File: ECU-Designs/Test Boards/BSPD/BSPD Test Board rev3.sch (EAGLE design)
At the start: 30 parts, among them X1 CONNECTOR-10

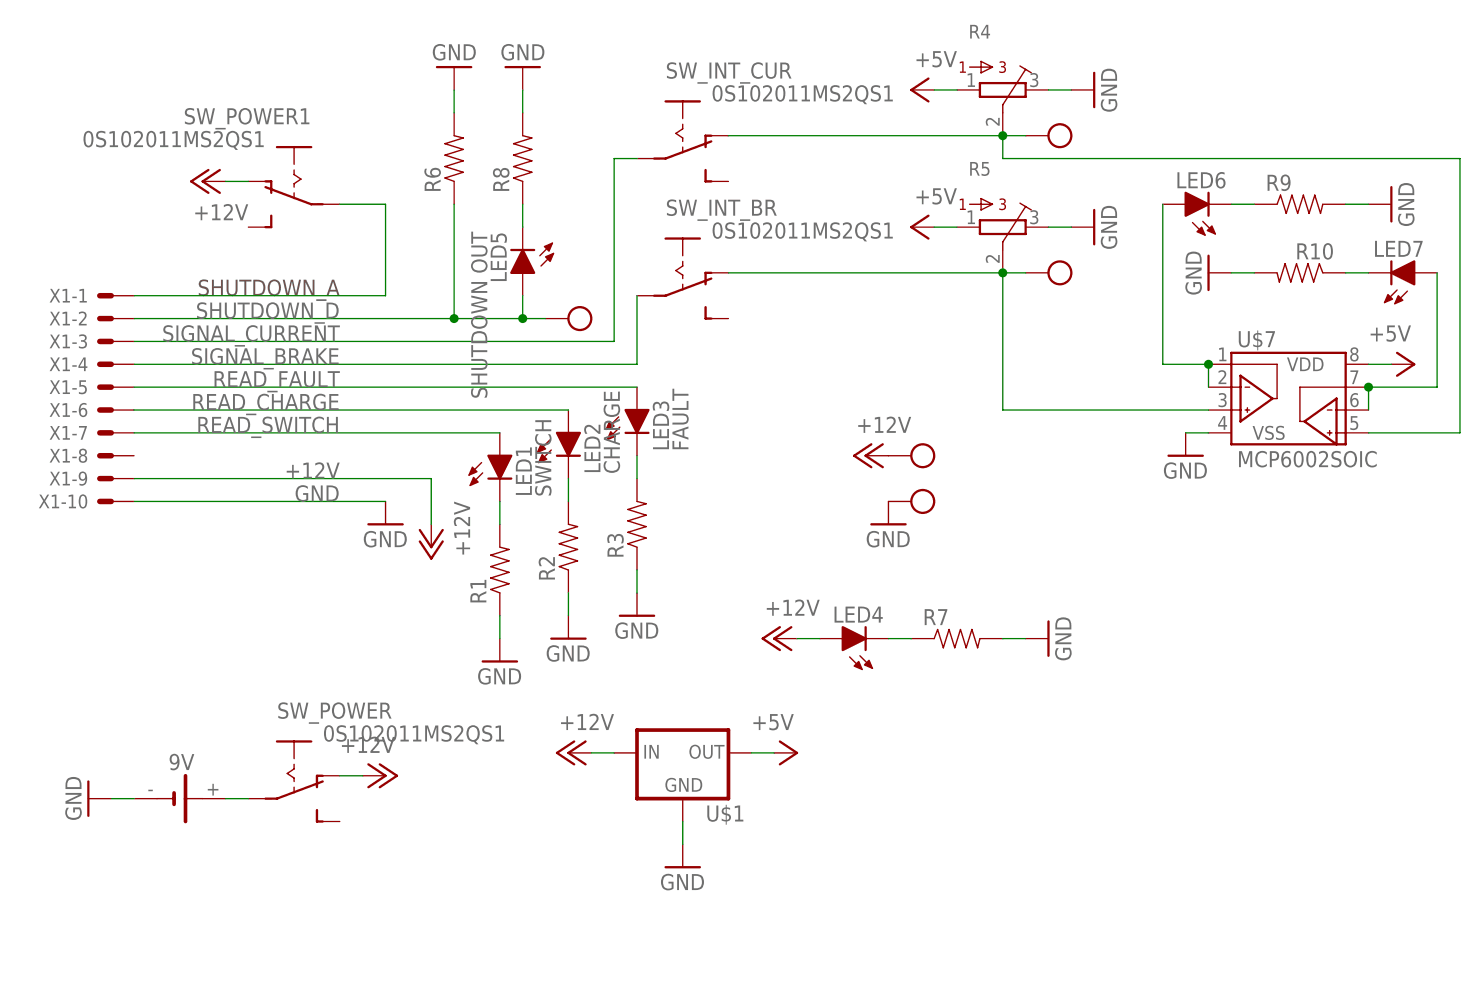
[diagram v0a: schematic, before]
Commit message: New versions of power board, bspd test board, can shield, bms adapter segment, bms shield
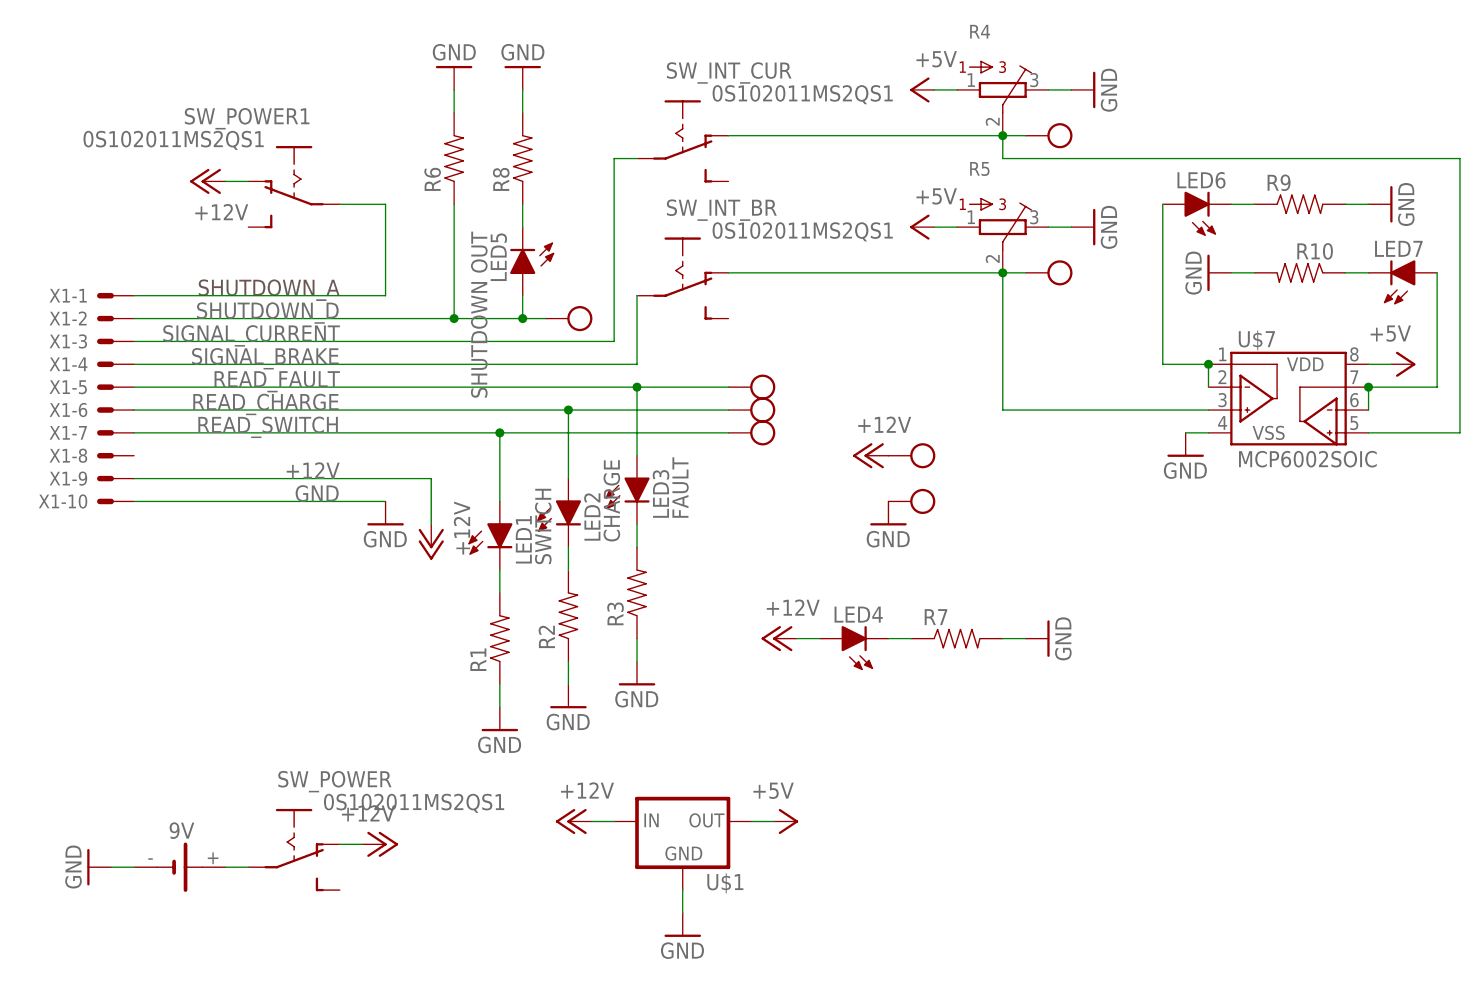
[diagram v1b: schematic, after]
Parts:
- added U$10, U$8, U$9: TEST_POINT, HyTechDevices:TEST_POINT
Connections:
- net READ_CHARGE: now also U$9.P$1
- net READ_FAULT: now also U$8.P$1
- net READ_SWITCH: now also U$10.P$1
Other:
- moved on the sheet: 9V, LED1, LED2, LED3, R1, R2, R3, SW_POWER, U$1
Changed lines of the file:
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@@
 <part name="SW_POWER1" library="HyTechDevices" deviceset="0S102011MS2QS1" device=""/>
 <part name="P+10" library="supply1" deviceset="+12V" device=""/>
+<part name="U$8" library="HyTechDevices" deviceset="TEST_POINT" device=""/>
+<part name="U$9" library="HyTechDevices" deviceset="TEST_POINT" device=""/>
+<part name="U$10" library="HyTechDevices" deviceset="TEST_POINT" device=""/>
 </parts>
 <sheets>
@@
 <instance part="X1" gate="-9" x="10.16" y="48.26" rot="MR0"/>
 <instance part="X1" gate="-10" x="10.16" y="45.72" rot="MR0"/>
-<instance part="LED1" gate="LED" x="53.34" y="50.8"/>
-<instance part="LED2" gate="LED" x="60.96" y="53.34"/>
-<instance part="LED3" gate="LED" x="68.58" y="55.88"/>
+<instance part="LED1" gate="LED" x="53.34" y="43.18"/>
+<instance part="LED2" gate="LED" x="60.96" y="45.72"/>
+<instance part="LED3" gate="LED" x="68.58" y="48.26"/>
 <instance part="GND1" gate="1" x="40.64" y="43.18"/>
 <instance part="P+1" gate="1" x="45.72" y="40.64" rot="R180"/>
-<instance part="R1" gate="G$1" x="53.34" y="38.1" rot="R90"/>
-<instance part="R2" gate="G$1" x="60.96" y="40.64" rot="R90"/>
-<instance part="R3" gate="G$1" x="68.58" y="43.18" rot="R90"/>
-<instance part="GND2" gate="1" x="53.34" y="27.94"/>
-<instance part="GND3" gate="1" x="60.96" y="30.48"/>
-<instance part="GND4" gate="1" x="68.58" y="33.02"/>
+<instance part="R1" gate="G$1" x="53.34" y="30.48" rot="R90"/>
+<instance part="R2" gate="G$1" x="60.96" y="33.02" rot="R90"/>
+<instance part="R3" gate="G$1" x="68.58" y="35.56" rot="R90"/>
+<instance part="GND2" gate="1" x="53.34" y="20.32"/>
+<instance part="GND3" gate="1" x="60.96" y="22.86"/>
+<instance part="GND4" gate="1" x="68.58" y="25.4"/>
 <instance part="R4" gate="G$1" x="109.22" y="91.44" rot="R270"/>
 <instance part="R5" gate="G$1" x="109.22" y="76.2" rot="R270"/>
 <instance part="GND5" gate="1" x="119.38" y="91.44" rot="R90"/>
 <instance part="GND6" gate="1" x="119.38" y="76.2" rot="R90"/>
-<instance part="P+4" gate="1" x="40.64" y="15.24" rot="R270"/>
-<instance part="GND7" gate="1" x="7.62" y="12.7" rot="R270"/>
-<instance part="U$1" gate="G$1" x="73.66" y="17.78"/>
-<instance part="P+5" gate="1" x="60.96" y="17.78" rot="MR270"/>
-<instance part="P+6" gate="1" x="86.36" y="17.78" rot="R270"/>
-<instance part="GND9" gate="1" x="73.66" y="5.08"/>
+<instance part="P+4" gate="1" x="40.64" y="7.62" rot="R270"/>
+<instance part="GND7" gate="1" x="7.62" y="5.08" rot="R270"/>
+<instance part="U$1" gate="G$1" x="73.66" y="10.16"/>
+<instance part="P+5" gate="1" x="60.96" y="10.16" rot="MR270"/>
+<instance part="P+6" gate="1" x="86.36" y="10.16" rot="R270"/>
+<instance part="GND9" gate="1" x="73.66" y="-2.54"/>
 <instance part="LED5" gate="LED" x="55.88" y="71.12" rot="R180"/>
 <instance part="R8" gate="G$1" x="55.88" y="83.82" rot="R90"/>
@@
 <instance part="SW_INT_CUR" gate="G$1" x="73.66" y="86.36" rot="R270"/>
 <instance part="SW_INT_BR" gate="G$1" x="73.66" y="71.12" rot="R270"/>
-<instance part="SW_POWER" gate="G$1" x="30.48" y="15.24" rot="R270"/>
+<instance part="SW_POWER" gate="G$1" x="30.48" y="7.62" rot="R270"/>
 <instance part="U$2" gate="G$1" x="114.3" y="86.36"/>
 <instance part="U$3" gate="G$1" x="114.3" y="71.12"/>
@@
 <instance part="R6" gate="G$1" x="48.26" y="83.82" rot="R90"/>
 <instance part="GND8" gate="1" x="48.26" y="93.98" rot="R180"/>
-<instance part="9V" gate="G$1" x="17.78" y="12.7"/>
+<instance part="9V" gate="G$1" x="17.78" y="5.08"/>
 <instance part="U$5" gate="G$1" x="99.06" y="50.8"/>
 <instance part="U$6" gate="G$1" x="99.06" y="45.72"/>
@@
 <instance part="SW_POWER1" gate="G$1" x="30.48" y="81.28" rot="MR270"/>
 <instance part="P+10" gate="1" x="20.32" y="81.28" rot="R90"/>
+<instance part="U$8" gate="G$1" x="81.28" y="58.42"/>
+<instance part="U$9" gate="G$1" x="81.28" y="55.88"/>
+<instance part="U$10" gate="G$1" x="81.28" y="53.34"/>
 </instances>
 <busses>
@@
 <segment>
 <pinref part="X1" gate="-5" pin="S"/>
-<wire x1="12.7" y1="58.42" x2="68.58" y2="58.42" width="0.1524" layer="91"/>
 <label x="35.56" y="58.42" size="1.778" layer="95" rot="MR0"/>
 <pinref part="LED3" gate="LED" pin="A"/>
+<wire x1="12.7" y1="58.42" x2="68.58" y2="58.42" width="0.1524" layer="91"/>
+<wire x1="68.58" y1="58.42" x2="68.58" y2="50.8" width="0.1524" layer="91"/>
+<pinref part="U$8" gate="G$1" pin="P$1"/>
+<wire x1="78.74" y1="58.42" x2="68.58" y2="58.42" width="0.1524" layer="91"/>
+<junction x="68.58" y="58.42"/>
 </segment>
 </net>
@@
 <segment>
 <pinref part="X1" gate="-6" pin="S"/>
-<wire x1="12.7" y1="55.88" x2="60.96" y2="55.88" width="0.1524" layer="91"/>
 <label x="35.56" y="55.88" size="1.778" layer="95" rot="MR0"/>
 <pinref part="LED2" gate="LED" pin="A"/>
+<wire x1="12.7" y1="55.88" x2="60.96" y2="55.88" width="0.1524" layer="91"/>
+<wire x1="60.96" y1="55.88" x2="60.96" y2="48.26" width="0.1524" layer="91"/>
+<pinref part="U$9" gate="G$1" pin="P$1"/>
+<wire x1="78.74" y1="55.88" x2="60.96" y2="55.88" width="0.1524" layer="91"/>
+<junction x="60.96" y="55.88"/>
 </segment>
 </net>
@@
 <segment>
 <pinref part="X1" gate="-7" pin="S"/>
-<wire x1="12.7" y1="53.34" x2="53.34" y2="53.34" width="0.1524" layer="91"/>
 <label x="35.56" y="53.34" size="1.778" layer="95" rot="MR0"/>
 <pinref part="LED1" gate="LED" pin="A"/>
+<wire x1="12.7" y1="53.34" x2="53.34" y2="53.34" width="0.1524" layer="91"/>
+<wire x1="53.34" y1="53.34" x2="53.34" y2="45.72" width="0.1524" layer="91"/>
+<pinref part="U$10" gate="G$1" pin="P$1"/>
+<wire x1="78.74" y1="53.34" x2="53.34" y2="53.34" width="0.1524" layer="91"/>
+<junction x="53.34" y="53.34"/>
 </segment>
 </net>
@@
 <segment>
 <pinref part="P+4" gate="1" pin="+12V"/>
-<wire x1="38.1" y1="15.24" x2="35.56" y2="15.24" width="0.1524" layer="91"/>
+<wire x1="38.1" y1="7.62" x2="35.56" y2="7.62" width="0.1524" layer="91"/>
 <pinref part="SW_POWER" gate="G$1" pin="O"/>
 </segment>
@@
 <pinref part="U$1" gate="G$1" pin="IN"/>
 <pinref part="P+5" gate="1" pin="+12V"/>
-<wire x1="63.5" y1="17.78" x2="66.04" y2="17.78" width="0.1524" layer="91"/>
+<wire x1="63.5" y1="10.16" x2="66.04" y2="10.16" width="0.1524" layer="91"/>
 </segment>
 <segment>
@@
 <pinref part="R1" gate="G$1" pin="1"/>
 <pinref part="GND2" gate="1" pin="GND"/>
-<wire x1="53.34" y1="30.48" x2="53.34" y2="33.02" width="0.1524" layer="91"/>
+<wire x1="53.34" y1="22.86" x2="53.34" y2="25.4" width="0.1524" layer="91"/>
 </segment>
 <segment>
 <pinref part="R2" gate="G$1" pin="1"/>
 <pinref part="GND3" gate="1" pin="GND"/>
-<wire x1="60.96" y1="33.02" x2="60.96" y2="35.56" width="0.1524" layer="91"/>
+<wire x1="60.96" y1="25.4" x2="60.96" y2="27.94" width="0.1524" layer="91"/>
 </segment>
 <segment>
 <pinref part="R3" gate="G$1" pin="1"/>
 <pinref part="GND4" gate="1" pin="GND"/>
-<wire x1="68.58" y1="35.56" x2="68.58" y2="38.1" width="0.1524" layer="91"/>
+<wire x1="68.58" y1="27.94" x2="68.58" y2="30.48" width="0.1524" layer="91"/>
 </segment>
 <segment>
@@
 <segment>
 <pinref part="GND7" gate="1" pin="GND"/>
-<wire x1="10.16" y1="12.7" x2="12.7" y2="12.7" width="0.1524" layer="91"/>
+<wire x1="10.16" y1="5.08" x2="12.7" y2="5.08" width="0.1524" layer="91"/>
 <pinref part="9V" gate="G$1" pin="-"/>
 </segment>
@@
 <pinref part="U$1" gate="G$1" pin="GND"/>
 <pinref part="GND9" gate="1" pin="GND"/>
-<wire x1="73.66" y1="7.62" x2="73.66" y2="10.16" width="0.1524" layer="91"/>
+<wire x1="73.66" y1="0" x2="73.66" y2="2.54" width="0.1524" layer="91"/>
 </segment>
 <segment>
@@
 <pinref part="LED1" gate="LED" pin="C"/>
 <pinref part="R1" gate="G$1" pin="2"/>
-<wire x1="53.34" y1="43.18" x2="53.34" y2="45.72" width="0.1524" layer="91"/>
+<wire x1="53.34" y1="35.56" x2="53.34" y2="38.1" width="0.1524" layer="91"/>
 </segment>
 </net>
@@
 <pinref part="LED2" gate="LED" pin="C"/>
 <pinref part="R2" gate="G$1" pin="2"/>
-<wire x1="60.96" y1="45.72" x2="60.96" y2="48.26" width="0.1524" layer="91"/>
+<wire x1="60.96" y1="38.1" x2="60.96" y2="40.64" width="0.1524" layer="91"/>
 </segment>
 </net>
@@
 <pinref part="LED3" gate="LED" pin="C"/>
 <pinref part="R3" gate="G$1" pin="2"/>
-<wire x1="68.58" y1="48.26" x2="68.58" y2="50.8" width="0.1524" layer="91"/>
+<wire x1="68.58" y1="40.64" x2="68.58" y2="43.18" width="0.1524" layer="91"/>
 </segment>
 </net>
@@
 <net name="N$6" class="0">
 <segment>
-<wire x1="22.86" y1="12.7" x2="25.4" y2="12.7" width="0.1524" layer="91"/>
+<wire x1="22.86" y1="5.08" x2="25.4" y2="5.08" width="0.1524" layer="91"/>
 <pinref part="SW_POWER" gate="G$1" pin="P"/>
 <pinref part="9V" gate="G$1" pin="+"/>
@@
 <pinref part="U$1" gate="G$1" pin="OUT"/>
 <pinref part="P+6" gate="1" pin="+5V"/>
-<wire x1="83.82" y1="17.78" x2="81.28" y2="17.78" width="0.1524" layer="91"/>
-</segment>
-<segment>
+<wire x1="83.82" y1="10.16" x2="81.28" y2="10.16" width="0.1524" layer="91"/>
+</segment>
+<segment>

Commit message: Added resistor values
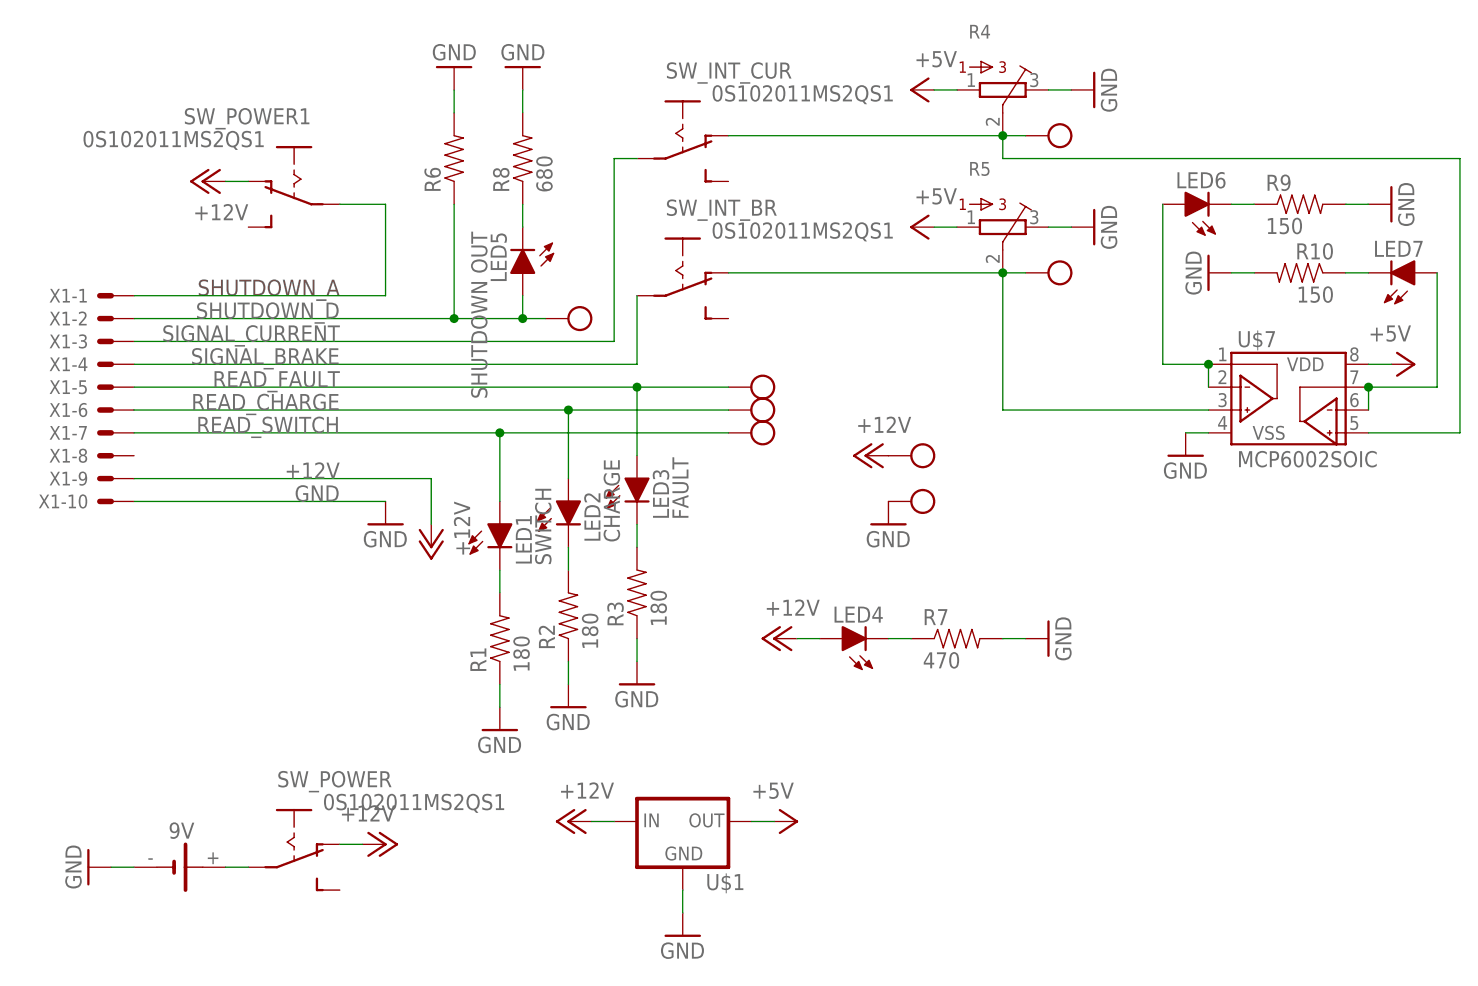
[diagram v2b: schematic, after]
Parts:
- R1, R2, R3: value (none) -> 180
- R10, R9: value (none) -> 150
- R7: value (none) -> 470
- R8: value (none) -> 680
